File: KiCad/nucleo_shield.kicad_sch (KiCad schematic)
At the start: 33 parts, among them J13 Conn_01x10_2,54mm, J4 Conn_01x08_2,54mm, J5 Conn_01x06_2,54mm, J7 Conn_01x08_2,54mm, J8 DC_Jack_2.5mm, U1 ADA4625-2ARDZ, U3 OPA197xD, U4 LD1117S50TR_SOT223

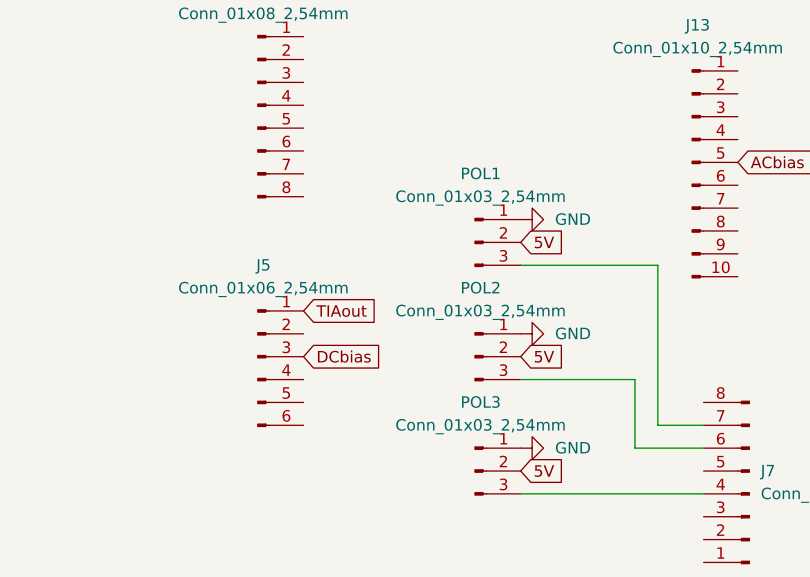
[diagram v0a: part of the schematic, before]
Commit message: added 12v source for nucleo
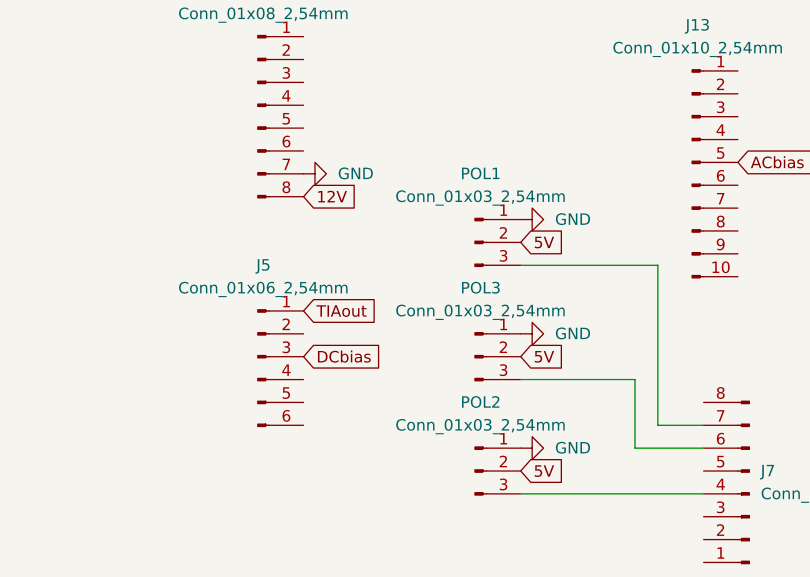
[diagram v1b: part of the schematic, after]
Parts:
- renumbered POL3 to POL2, POL2 to POL3
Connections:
- net 12V: now also J4.8 (Pin_8)
- net GND: now also J4.7 (Pin_7)
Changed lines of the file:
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@@
+		)
+	)
+	(global_label "12V"
+		(shape input)
+		(at 104.14 36.83 0)
+		(fields_autoplaced yes)
+		(effects
+			(font
+				(size 1.27 1.27)
+			)
+			(justify left)
+		)
+		(property "Intersheetrefs" "${INTERSHEET_REFS}"
+			(at 109.9786 36.83 0)
+			(effects
+				(font
+					(size 1.27 1.27)
+				)
+				(justify left)
+				(hide yes)
+			)
 		)
 	)
@@
 		(dnp no)
 		(fields_autoplaced yes)
-		(property "Reference" "POL3"
+		(property "Reference" "POL2"
 			(at 123.825 59.69 0)
 			(effects
@@
 			(project "MIP_Template"
 				(path "/0a653fc0-4dea-47e5-b804-9bb7e8c31233"
-					(reference "POL3")
+					(reference "POL2")
 					(unit 1)
 				)
@@
 		(dnp no)
 		(fields_autoplaced yes)
-		(property "Reference" "POL2"
+		(property "Reference" "POL3"
 			(at 123.825 46.99 0)
 			(effects
@@
 			(project "MIP_Template"
 				(path "/0a653fc0-4dea-47e5-b804-9bb7e8c31233"
-					(reference "POL2")
+					(reference "POL3")
 					(unit 1)
 				)
@@
 					(unit 1)
 				)
+			)
+		)
+	)
+	(symbol
+		(lib_id "power:GND")
+		(at 104.14 34.29 90)
+		(unit 1)
+		(exclude_from_sim no)
+		(in_bom yes)
+		(on_board yes)
+		(dnp no)
+		(fields_autoplaced yes)
+		(property "Reference" "#PWR05"
+			(at 110.49 34.29 0)
+			(effects
+				(font
+					(size 1.27 1.27)
+				)
+				(hide yes)
+			)
+		)
+		(property "Value" "GND"
+			(at 107.95 34.2899 90)
+			(effects
+				(font
+					(size 1.27 1.27)
+				)
+				(justify right)
+			)
+		)
+		(property "Footprint" ""
+			(at 104.14 34.29 0)
+			(effects
+				(font
+					(size 1.27 1.27)
+				)
+				(hide yes)
+			)
+		)
+		(property "Datasheet" ""
+			(at 104.14 34.29 0)
+			(effects
+				(font
+					(size 1.27 1.27)
+				)
+				(hide yes)
+			)
+		)
+		(property "Description" "Power symbol creates a global label with name \"GND\" , ground"
+			(at 104.14 34.29 0)
+			(effects
+				(font
+					(size 1.27 1.27)
+				)
+				(hide yes)
+			)
+		)
+		(pin "1"
+		)
+		(instances
+			(project "nucleo_shield"
+				(path "/0a653fc0-4dea-47e5-b804-9bb7e8c31233"
+					(reference "#PWR05")
+					(unit 1)
+				)
